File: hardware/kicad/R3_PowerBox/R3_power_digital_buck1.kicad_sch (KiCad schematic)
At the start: 10 parts, among them U1 TPS62132RGTR

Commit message: Finalize R3 PowerBox pre-placement corrections
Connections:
- net N$12 renamed N$11
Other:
- moved on the sheet: C10, C11, C12, C13, C14, U1

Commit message: Finalize R3 PowerBox pre-routing placement
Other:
- moved on the sheet: L1, R10

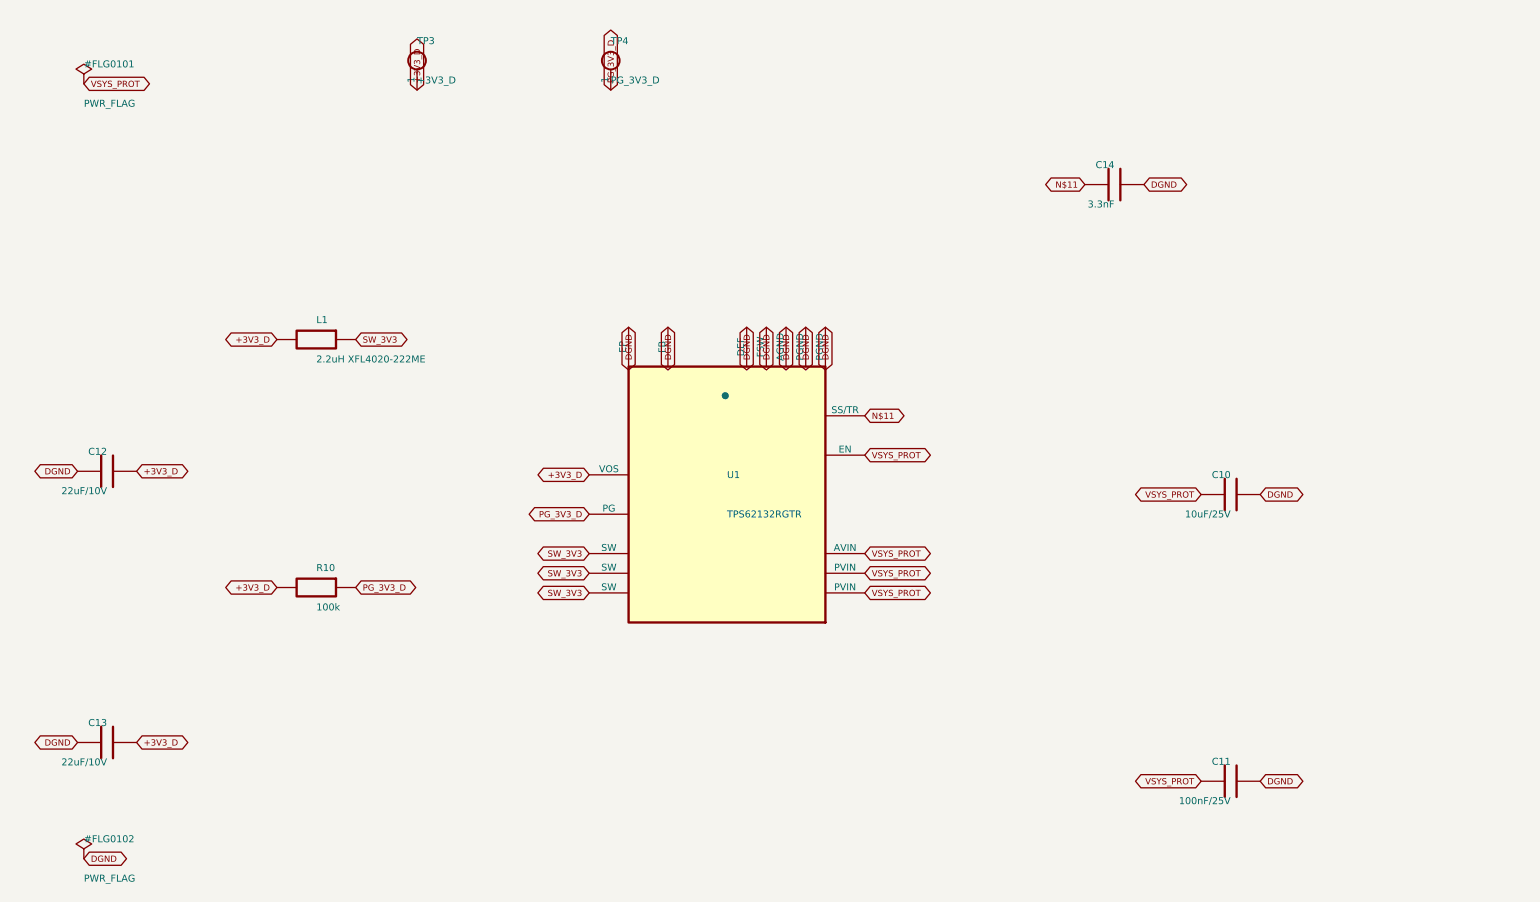
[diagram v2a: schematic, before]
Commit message: Finalize R3 PowerBox user power controls
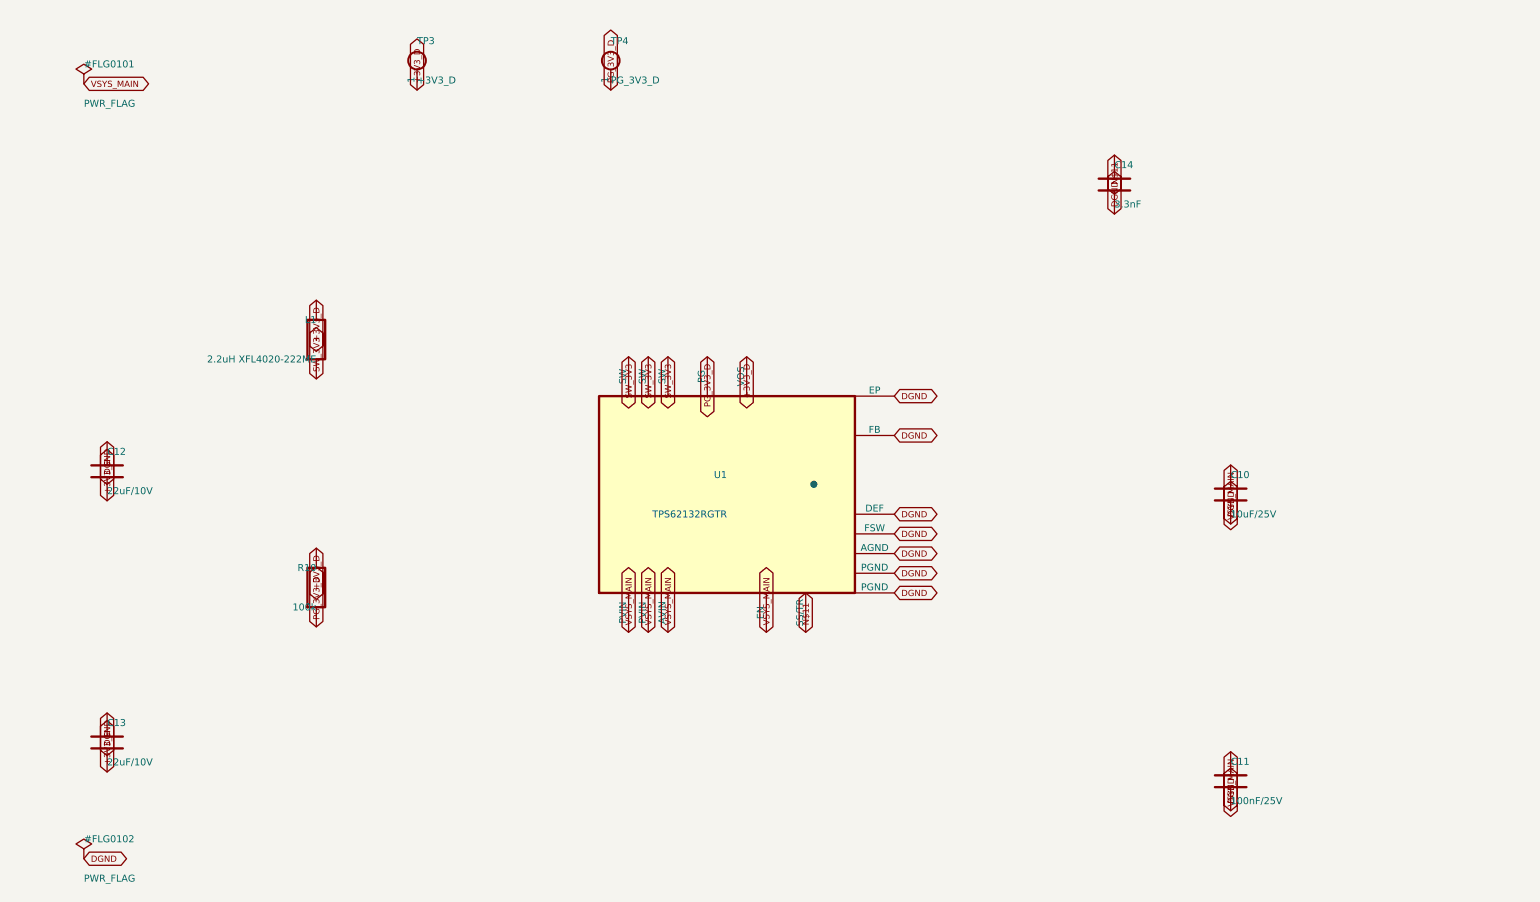
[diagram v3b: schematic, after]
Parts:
- U1: footprint Package_DFN_QFN:VQFN-16-1EP_3x3mm_P0.5mm_EP1.45x1.45mm_ThermalVias -> Package_DFN_QFN:VQFN-16-1EP_3x3mm_P0.5mm_EP1.45x1.45mm
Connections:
- net VSYS_PROT renamed VSYS_MAIN
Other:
- moved on the sheet: C10, C11, C12, C13, C14, L1, R10, U1

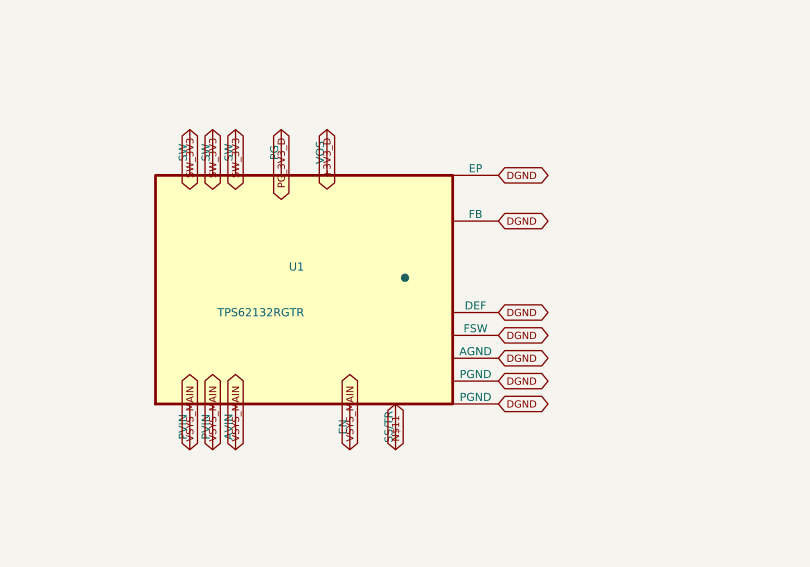
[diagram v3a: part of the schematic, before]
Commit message: Finalize R3 PowerBox mechanical interconnect
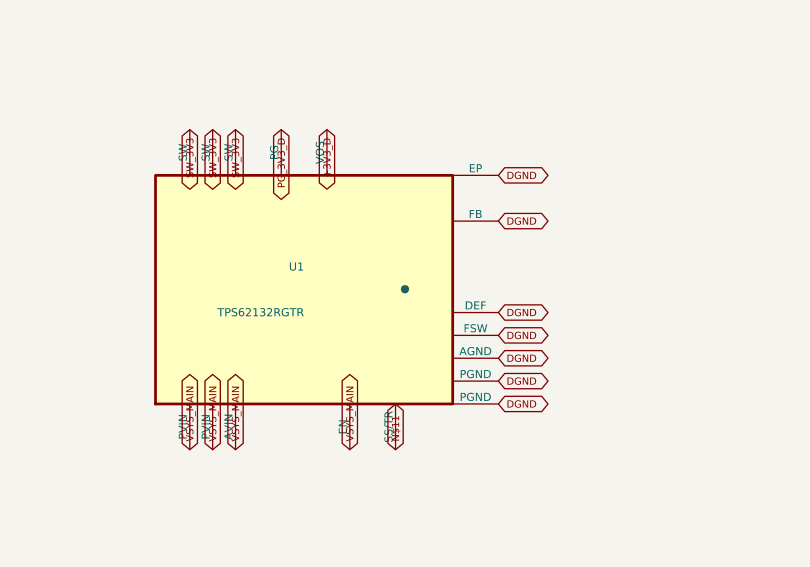
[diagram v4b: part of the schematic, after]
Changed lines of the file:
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@@
     (instances
       (project "SKiDL-Generated"
-        (path "/ed43c75e-de56-4b8e-bb37-9a897af3b629/690ee384-44a1-5a13-b84c-258c10c7482c"
+        (path "/9be6bff1-dc85-4a48-94a9-d7223c5e518f/690ee384-44a1-5a13-b84c-258c10c7482c"
           (reference "#FLG0101")
           (unit 1)))))
@@
     (instances
       (project "SKiDL-Generated"
-        (path "/ed43c75e-de56-4b8e-bb37-9a897af3b629/690ee384-44a1-5a13-b84c-258c10c7482c"
+        (path "/9be6bff1-dc85-4a48-94a9-d7223c5e518f/690ee384-44a1-5a13-b84c-258c10c7482c"
           (reference "#FLG0102")
           (unit 1)))))
@@
     (instances
       (project "SKiDL-Generated"
-        (path "/ed43c75e-de56-4b8e-bb37-9a897af3b629/690ee384-44a1-5a13-b84c-258c10c7482c"
+        (path "/9be6bff1-dc85-4a48-94a9-d7223c5e518f/690ee384-44a1-5a13-b84c-258c10c7482c"
           (reference "U1")
           (unit 1)))))
@@
     (instances
       (project "SKiDL-Generated"
-        (path "/ed43c75e-de56-4b8e-bb37-9a897af3b629/690ee384-44a1-5a13-b84c-258c10c7482c"
+        (path "/9be6bff1-dc85-4a48-94a9-d7223c5e518f/690ee384-44a1-5a13-b84c-258c10c7482c"
           (reference "L1")
           (unit 1)))))
@@
     (instances
       (project "SKiDL-Generated"
-        (path "/ed43c75e-de56-4b8e-bb37-9a897af3b629/690ee384-44a1-5a13-b84c-258c10c7482c"
+        (path "/9be6bff1-dc85-4a48-94a9-d7223c5e518f/690ee384-44a1-5a13-b84c-258c10c7482c"
           (reference "C10")
           (unit 1)))))
@@
     (instances
       (project "SKiDL-Generated"
-        (path "/ed43c75e-de56-4b8e-bb37-9a897af3b629/690ee384-44a1-5a13-b84c-258c10c7482c"
+        (path "/9be6bff1-dc85-4a48-94a9-d7223c5e518f/690ee384-44a1-5a13-b84c-258c10c7482c"
           (reference "C11")
           (unit 1)))))
@@
     (instances
       (project "SKiDL-Generated"
-        (path "/ed43c75e-de56-4b8e-bb37-9a897af3b629/690ee384-44a1-5a13-b84c-258c10c7482c"
+        (path "/9be6bff1-dc85-4a48-94a9-d7223c5e518f/690ee384-44a1-5a13-b84c-258c10c7482c"
           (reference "C12")
           (unit 1)))))
@@
     (instances
       (project "SKiDL-Generated"
-        (path "/ed43c75e-de56-4b8e-bb37-9a897af3b629/690ee384-44a1-5a13-b84c-258c10c7482c"
+        (path "/9be6bff1-dc85-4a48-94a9-d7223c5e518f/690ee384-44a1-5a13-b84c-258c10c7482c"
           (reference "C13")
           (unit 1)))))
@@
     (instances
       (project "SKiDL-Generated"
-        (path "/ed43c75e-de56-4b8e-bb37-9a897af3b629/690ee384-44a1-5a13-b84c-258c10c7482c"
+        (path "/9be6bff1-dc85-4a48-94a9-d7223c5e518f/690ee384-44a1-5a13-b84c-258c10c7482c"
           (reference "C14")
           (unit 1)))))
@@
     (instances
       (project "SKiDL-Generated"
-        (path "/ed43c75e-de56-4b8e-bb37-9a897af3b629/690ee384-44a1-5a13-b84c-258c10c7482c"
+        (path "/9be6bff1-dc85-4a48-94a9-d7223c5e518f/690ee384-44a1-5a13-b84c-258c10c7482c"
           (reference "R10")
           (unit 1)))))
@@
     (instances
       (project "SKiDL-Generated"
-        (path "/ed43c75e-de56-4b8e-bb37-9a897af3b629/690ee384-44a1-5a13-b84c-258c10c7482c"
+        (path "/9be6bff1-dc85-4a48-94a9-d7223c5e518f/690ee384-44a1-5a13-b84c-258c10c7482c"
           (reference "TP3")
           (unit 1)))))
@@
     (instances
       (project "SKiDL-Generated"
-        (path "/ed43c75e-de56-4b8e-bb37-9a897af3b629/690ee384-44a1-5a13-b84c-258c10c7482c"
+        (path "/9be6bff1-dc85-4a48-94a9-d7223c5e518f/690ee384-44a1-5a13-b84c-258c10c7482c"
           (reference "TP4")
           (unit 1)))))
   (junction
-    (at 156.21 106.68)
+    (at 156.21 107.95)
     (diameter 0)
     (color 0 0 0 0)

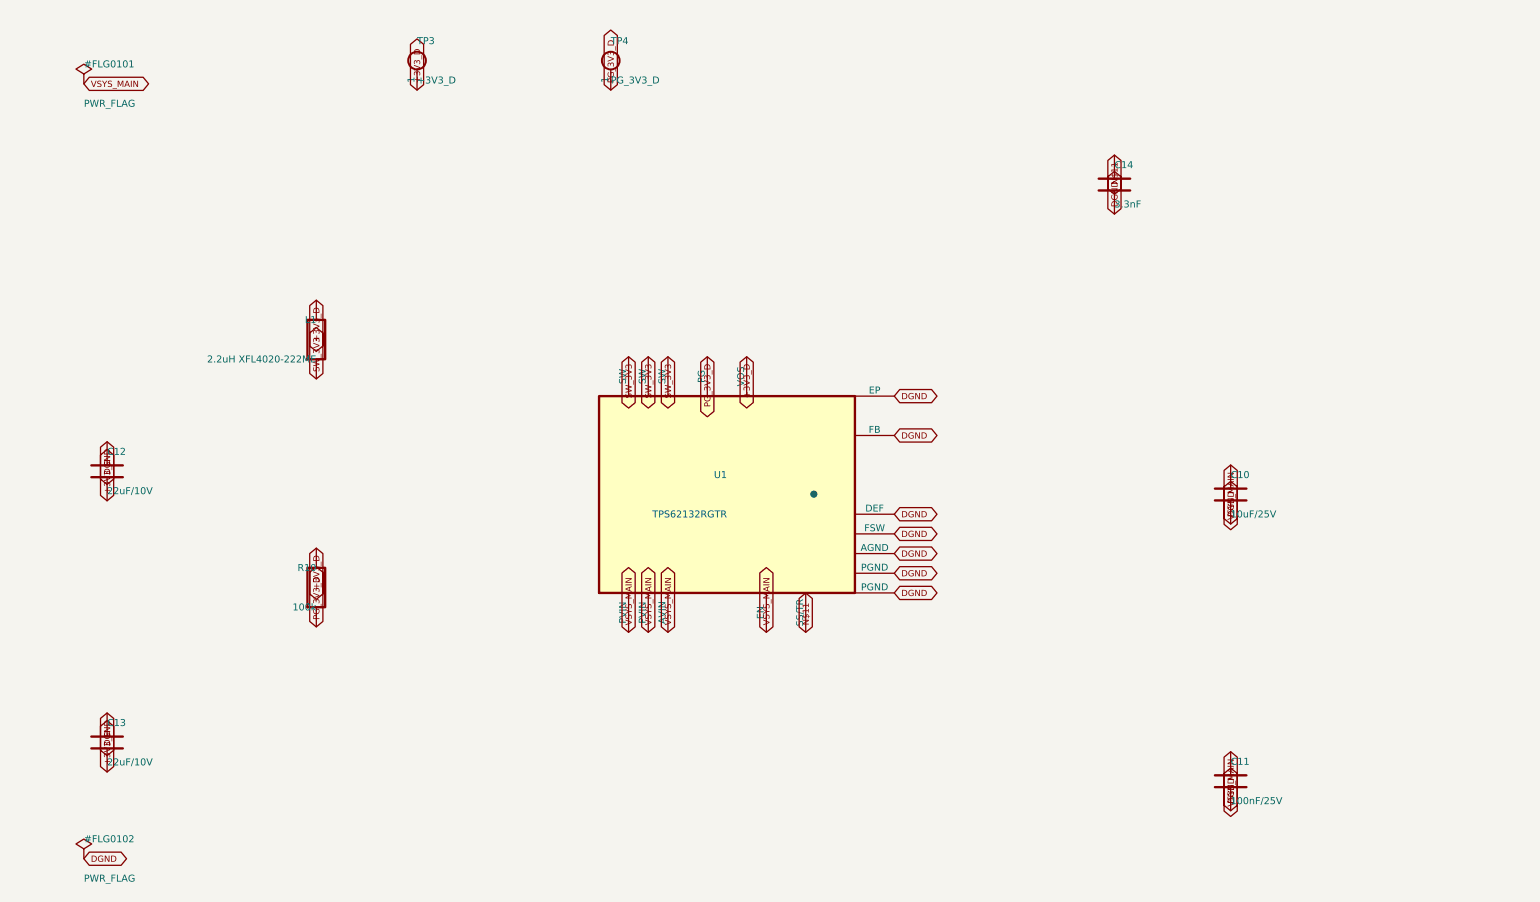
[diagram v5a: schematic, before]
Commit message: Rev.A review fixes: initial schematic and component corrections
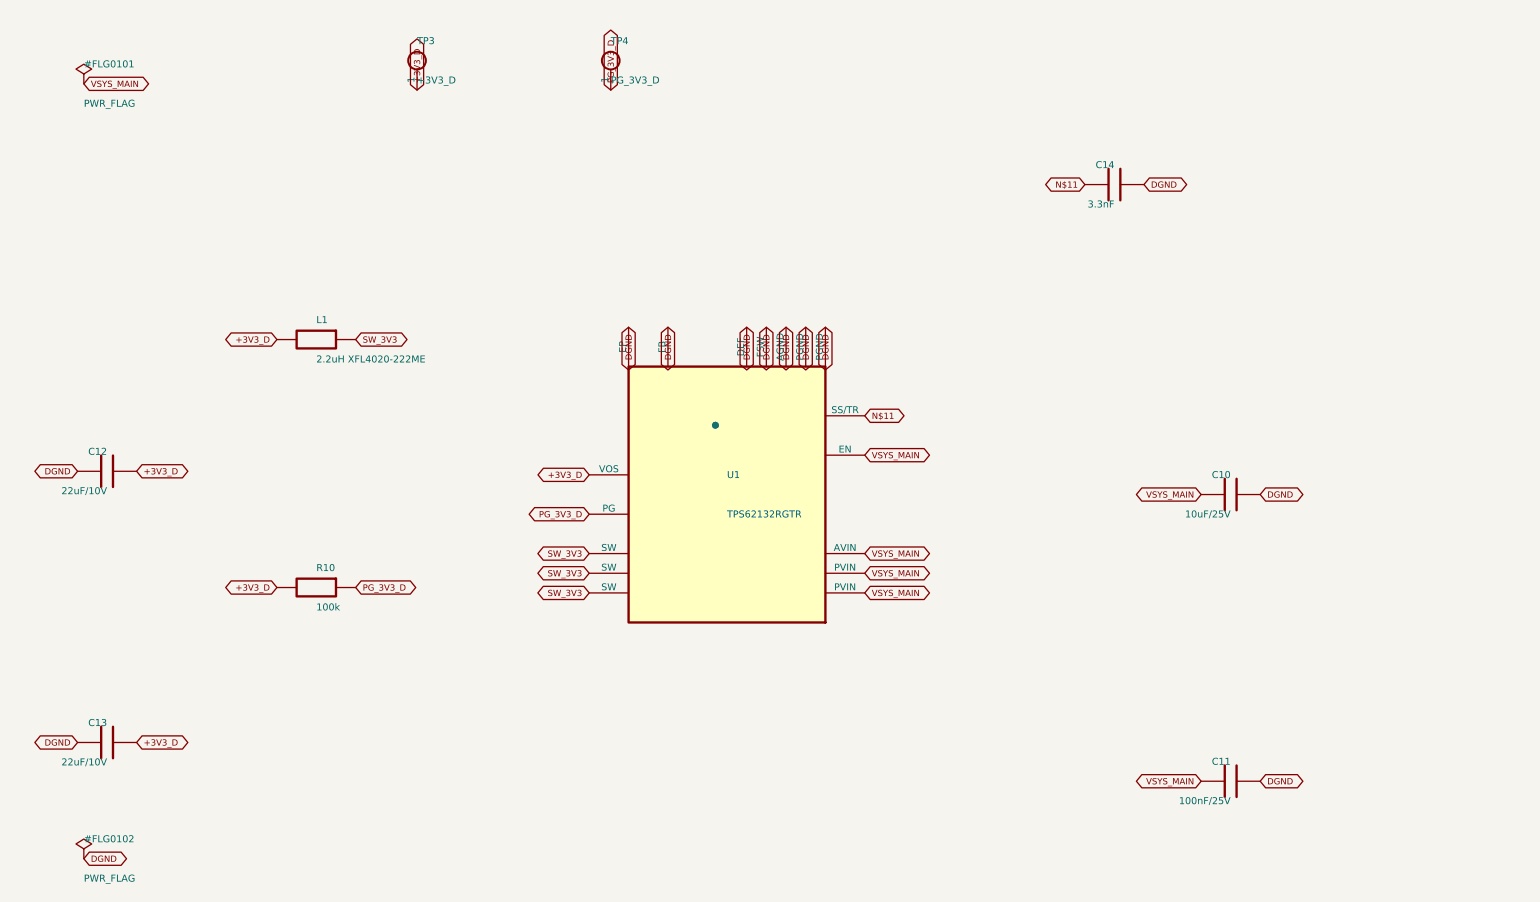
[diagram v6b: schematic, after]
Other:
- moved on the sheet: C10, C11, C12, C13, C14, L1, R10, U1

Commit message: Rev.A review fixes: local charger power-stage reroute checkpoint
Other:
- moved on the sheet: C10, C11, C12, C13, C14, L1, R10, U1

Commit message: Rev.A review fixes: final CAD verification and documented hardware gates
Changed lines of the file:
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@@
+		)
+	)
+	(global_label "+3V3_D"
+		(shape bidirectional)
+		(at 240 55 0)
+		(effects
+			(font
+				(size 0.8 0.8)
+			)
+			(justify left)
 		)
 	)
@@
     (instances
       (project "SKiDL-Generated"
-        (path "/2b0a7443-ac4c-4207-8273-267cee2a0847/690ee384-44a1-5a13-b84c-258c10c7482c"
+        (path "/9d9979b9-42ef-4da5-ae7f-11c414f8c896/690ee384-44a1-5a13-b84c-258c10c7482c"
           (reference "#FLG0101")
           (unit 1)))))
@@
     (instances
       (project "SKiDL-Generated"
-        (path "/2b0a7443-ac4c-4207-8273-267cee2a0847/690ee384-44a1-5a13-b84c-258c10c7482c"
+        (path "/9d9979b9-42ef-4da5-ae7f-11c414f8c896/690ee384-44a1-5a13-b84c-258c10c7482c"
           (reference "#FLG0102")
           (unit 1)))))
@@
     (instances
       (project "SKiDL-Generated"
-        (path "/2b0a7443-ac4c-4207-8273-267cee2a0847/690ee384-44a1-5a13-b84c-258c10c7482c"
+        (path "/9d9979b9-42ef-4da5-ae7f-11c414f8c896/690ee384-44a1-5a13-b84c-258c10c7482c"
           (reference "U1")
           (unit 1)))))
@@
     (instances
       (project "SKiDL-Generated"
-        (path "/2b0a7443-ac4c-4207-8273-267cee2a0847/690ee384-44a1-5a13-b84c-258c10c7482c"
+        (path "/9d9979b9-42ef-4da5-ae7f-11c414f8c896/690ee384-44a1-5a13-b84c-258c10c7482c"
           (reference "L1")
+          (unit 1)))))
+  (symbol
+    (lib_id "power:PWR_FLAG")
+    (at 240 55 0)
+    (unit 1)
+    (exclude_from_sim no)
+    (in_bom yes)
+    (on_board yes)
+    (dnp no)
+    (fields_autoplaced yes)
+    (property "Reference" "#FLG0103"
+      (at 240 52.46 0)
+      (effects
+        (font
+          (size 0.9 0.9))
+        (justify left)))
+    (property "Value" "PWR_FLAG"
+      (at 240 57.54 0)
+      (effects
+        (font
+          (size 0.9 0.9))
+        (justify left)))
+    (property "Footprint" ""
+      (at 240 55 0)
+      (effects
+        (font
+          (size 0.9 0.9))
+        (hide yes)))
+    (property "Datasheet" "~"
+      (at 240 55 0)
+      (effects
+        (font
+          (size 0.9 0.9))
+        (hide yes)))
+    (property "Description" "Special symbol for telling ERC where power comes from"
+      (at 240 55 0)
+      (effects
+        (font
+          (size 0.9 0.9))
+        (hide yes)))
+    (pin "1"
+)
+    (instances
+      (project "SKiDL-Generated"
+        (path "/9d9979b9-42ef-4da5-ae7f-11c414f8c896/690ee384-44a1-5a13-b84c-258c10c7482c"
+          (reference "#FLG0103")
           (unit 1)))))
   (symbol
@@
     (instances
       (project "SKiDL-Generated"
-        (path "/2b0a7443-ac4c-4207-8273-267cee2a0847/690ee384-44a1-5a13-b84c-258c10c7482c"
+        (path "/9d9979b9-42ef-4da5-ae7f-11c414f8c896/690ee384-44a1-5a13-b84c-258c10c7482c"
           (reference "C10")
           (unit 1)))))
@@
     (instances
       (project "SKiDL-Generated"
-        (path "/2b0a7443-ac4c-4207-8273-267cee2a0847/690ee384-44a1-5a13-b84c-258c10c7482c"
+        (path "/9d9979b9-42ef-4da5-ae7f-11c414f8c896/690ee384-44a1-5a13-b84c-258c10c7482c"
           (reference "C11")
           (unit 1)))))
@@
     (instances
       (project "SKiDL-Generated"
-        (path "/2b0a7443-ac4c-4207-8273-267cee2a0847/690ee384-44a1-5a13-b84c-258c10c7482c"
+        (path "/9d9979b9-42ef-4da5-ae7f-11c414f8c896/690ee384-44a1-5a13-b84c-258c10c7482c"
           (reference "C12")
           (unit 1)))))
@@
     (instances
       (project "SKiDL-Generated"
-        (path "/2b0a7443-ac4c-4207-8273-267cee2a0847/690ee384-44a1-5a13-b84c-258c10c7482c"
+        (path "/9d9979b9-42ef-4da5-ae7f-11c414f8c896/690ee384-44a1-5a13-b84c-258c10c7482c"
           (reference "C13")
           (unit 1)))))
@@
     (instances
       (project "SKiDL-Generated"
-        (path "/2b0a7443-ac4c-4207-8273-267cee2a0847/690ee384-44a1-5a13-b84c-258c10c7482c"
+        (path "/9d9979b9-42ef-4da5-ae7f-11c414f8c896/690ee384-44a1-5a13-b84c-258c10c7482c"
           (reference "C14")
           (unit 1)))))
@@
     (instances
       (project "SKiDL-Generated"
-        (path "/2b0a7443-ac4c-4207-8273-267cee2a0847/690ee384-44a1-5a13-b84c-258c10c7482c"
+        (path "/9d9979b9-42ef-4da5-ae7f-11c414f8c896/690ee384-44a1-5a13-b84c-258c10c7482c"
           (reference "R10")
           (unit 1)))))
@@
     (instances
       (project "SKiDL-Generated"
-        (path "/2b0a7443-ac4c-4207-8273-267cee2a0847/690ee384-44a1-5a13-b84c-258c10c7482c"
+        (path "/9d9979b9-42ef-4da5-ae7f-11c414f8c896/690ee384-44a1-5a13-b84c-258c10c7482c"
           (reference "TP3")
           (unit 1)))))
@@
     (instances
       (project "SKiDL-Generated"
-        (path "/2b0a7443-ac4c-4207-8273-267cee2a0847/690ee384-44a1-5a13-b84c-258c10c7482c"
+        (path "/9d9979b9-42ef-4da5-ae7f-11c414f8c896/690ee384-44a1-5a13-b84c-258c10c7482c"
           (reference "TP4")
           (unit 1)))))
   (junction
-    (at 152.4 110.49)
+    (at 147.32 110.49)
     (diameter 0)
     (color 0 0 0 0)
